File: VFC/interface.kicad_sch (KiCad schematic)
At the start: 5 parts, among them J2 Conn_01x06_Socket, J3 Conn_01x06_Socket, J4 Conn_01x03_Socket, J5 Conn_01x04_Socket, J6 SM08B-SRSS-TB_LF__SN_

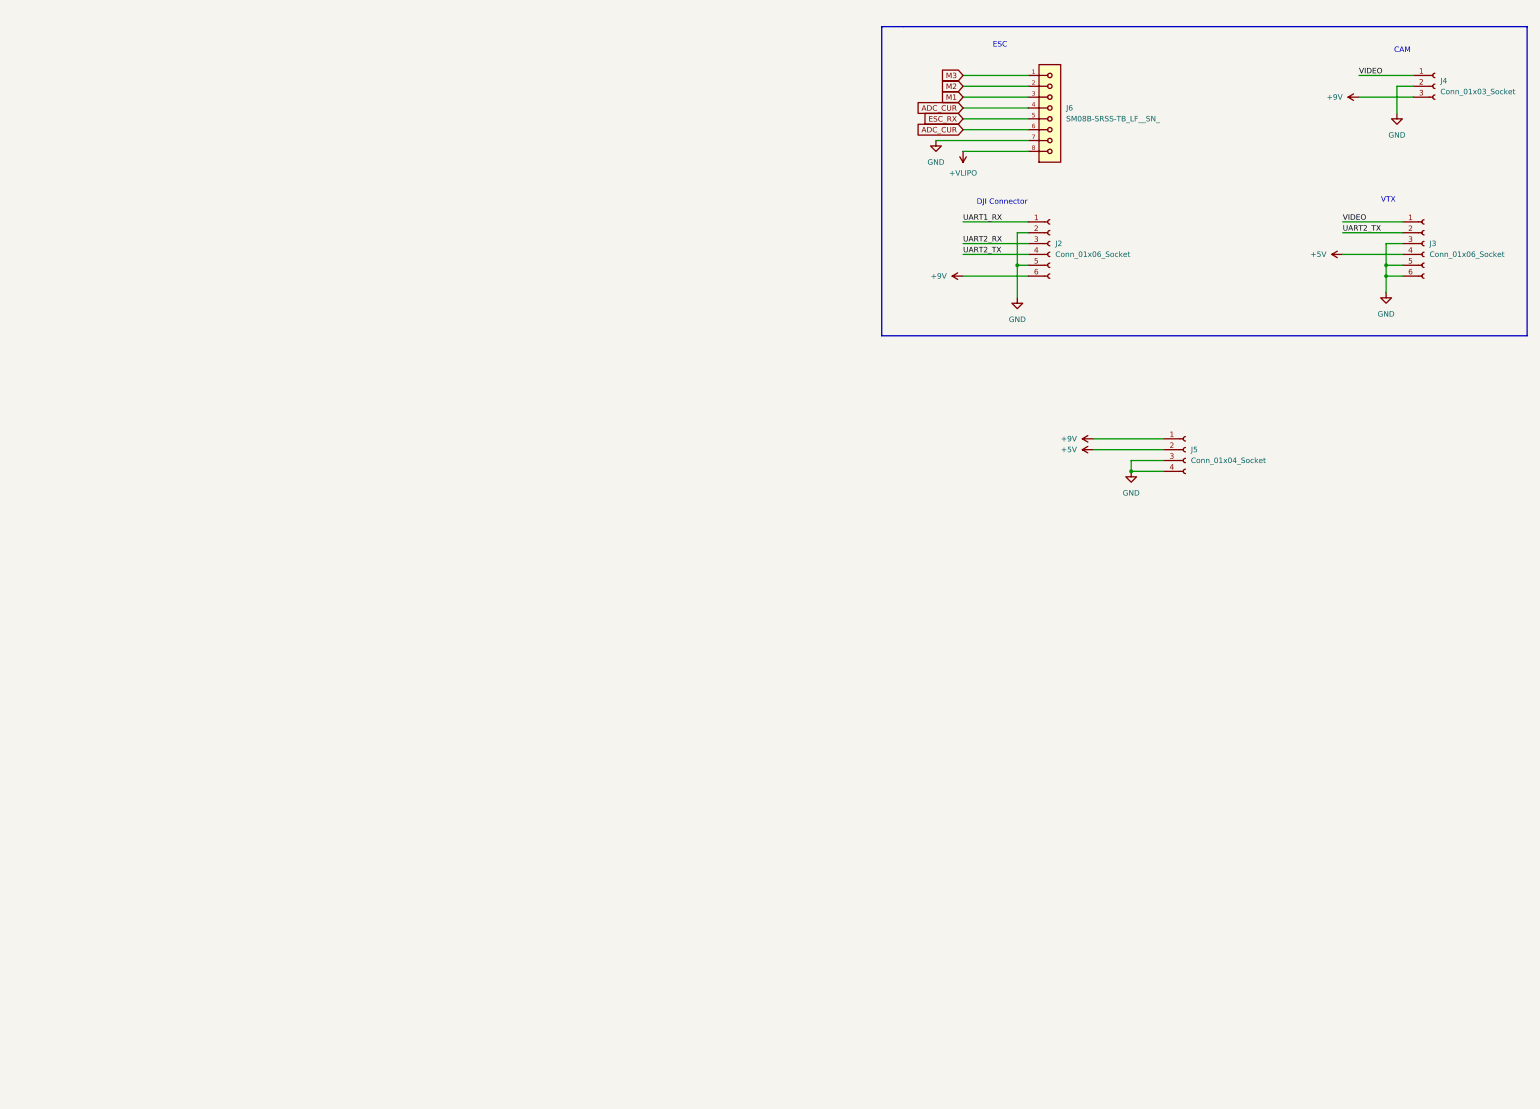
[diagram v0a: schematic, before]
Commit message: VFC PCB components placements complete
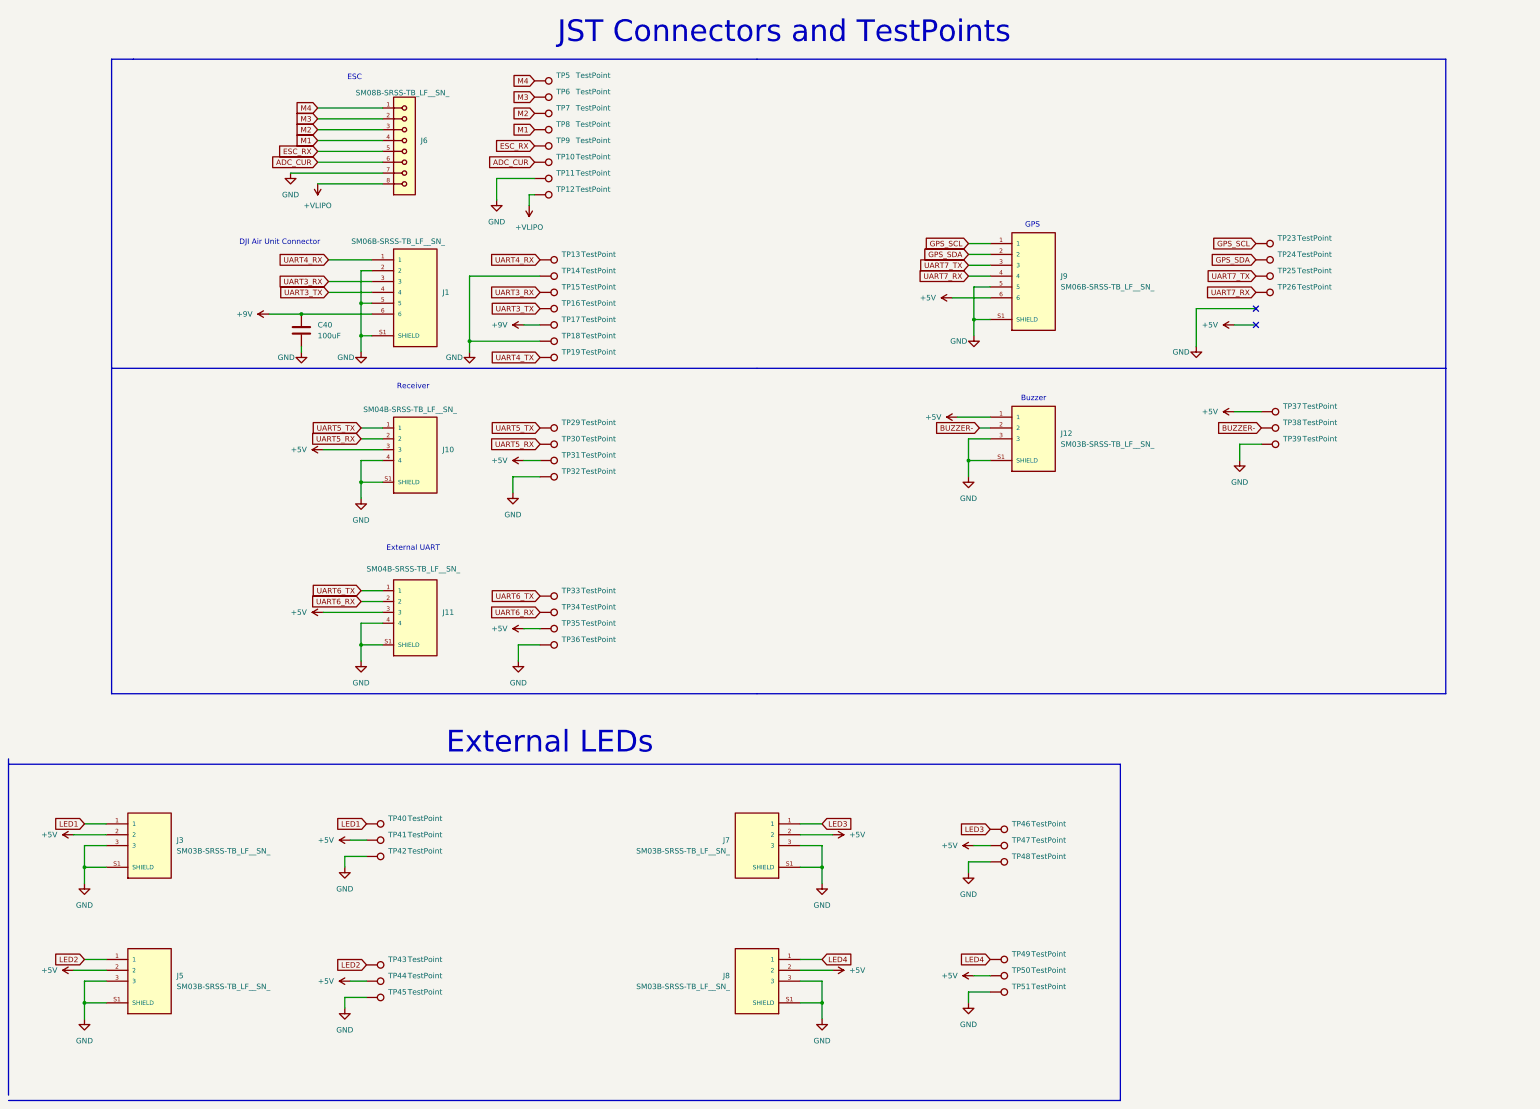
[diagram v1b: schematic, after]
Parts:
- removed J2, J3: Conn_01x06_Socket, Connector_JST:JST_SH_SM06B-SRSS-TB_1x06-1MP_P1.00mm_Horizontal, symbol Connector:Conn_01x06_Socket
- removed J4: Conn_01x03_Socket, Connector_JST:JST_SH_SM03B-SRSS-TB_1x03-1MP_P1.00mm_Horizontal, symbol Connector:Conn_01x03_Socket
- removed J5: Conn_01x04_Socket, symbol Connector:Conn_01x04_Socket
- added C40: 100uF, Capacitor_SMD:C_0603_1608Metric, symbol Device:C
- added J1, J9: SM06B-SRSS-TB_LF__SN_, SM06B-SRSS-TB_LF__SN_:JST_SM06B-SRSS-TB_LF__SN_, symbol SM06B-SRSS-TB_LF__SN_:SM06B-SRSS-TB_LF__SN_
- added J10, J11: SM04B-SRSS-TB_LF__SN_, SM04B-SRSS-TB_LF__SN_:JST_SM04B-SRSS-TB_LF__SN_, symbol SM04B-SRSS-TB_LF__SN_:SM04B-SRSS-TB_LF__SN_
- added J12, J3, J5, J7, J8: SM03B-SRSS-TB_LF__SN_, SM03B-SRSS-TB_LF__SN_:JST_SM03B-SRSS-TB_LF__SN_, symbol SM03B-SRSS-TB_LF__SN_:SM03B-SRSS-TB_LF__SN_
- added TP10, TP40, TP41, TP42, TP43, TP44, TP45, TP46, TP47, TP48, TP49, TP5, TP50, TP51, TP6, TP7, TP8, TP9: TestPoint, TestPoint:TestPoint_Pad_D1.0mm, symbol Connector:TestPoint
- added TP11, TP12: TestPoint, TestPoint:TestPoint_Pad_D2.0mm, symbol Connector:TestPoint
- added TP13, TP14, TP15, TP16, TP18, TP19, TP23, TP24, TP25, TP26, TP29, TP30, TP32, TP33, TP34, TP36, TP38, TP39: TestPoint, TestPoint:TestPoint_Pad_1.0x1.0mm, symbol Connector:TestPoint
- added TP17, TP31, TP35, TP37: TestPoint, TestPoint:TestPoint_Pad_2.0x2.0mm, symbol Connector:TestPoint
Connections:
- net +5V: now also J10.3, J11.3, J12.1, J3.2, J5.2, J7.2, J8.2, J9.6, TP31.1, TP35.1, TP37.1, TP41.1, TP44.1, TP47.1, TP50.1
- net +9V: now also C40.1, J1.6, TP17.1
- net +VLIPO: now also TP12.1
- net ADC_CUR: now also TP10.1; no longer J6.4
- net ESC_RX: now also TP9.1
- net GND: now also C40.2, J1.2, J1.5, J1.S1 (SHIELD), J1.S2 (SHIELD), J10.4, J10.S1 (SHIELD), J10.S2 (SHIELD), J11.4, J11.S1 (SHIELD), J11.S2 (SHIELD), J12.3, J12.S1 (SHIELD), J12.S2 (SHIELD), J3.3, J3.S1 (SHIELD), J3.S2 (SHIELD), J5.3, J5.S1 (SHIELD), J5.S2 (SHIELD), J7.3, J7.S1 (SHIELD), J7.S2 (SHIELD), J8.3, J8.S1 (SHIELD), J8.S2 (SHIELD), J9.5, J9.S1 (SHIELD), J9.S2 (SHIELD), TP11.1, TP14.1, TP18.1, TP32.1, TP36.1, TP39.1, TP42.1, TP45.1, TP48.1, TP51.1
- net M1: now also J6.4, TP8.1; no longer J6.3
- net M2: now also J6.3, TP7.1; no longer J6.2
- net M3: now also J6.2, TP6.1; no longer J6.1
- new net BUZZER-: J12.2, TP38.1
- new net GPS_SCL: J9.1, TP23.1
- new net GPS_SDA: J9.2, TP24.1
- new net LED1: J3.1, TP40.1
- new net LED2: J5.1, TP43.1
- new net LED3: J7.1, TP46.1
- new net LED4: J8.1, TP49.1
- new net M4: J6.1, TP5.1
- new net UART3_RX: J1.3, TP15.1
- new net UART3_TX: J1.4, TP16.1
- new net UART4_RX: J1.1, TP13.1
- new net UART4_TX: TP19.1
- new net UART5_RX: J10.2, TP30.1
- new net UART5_TX: J10.1, TP29.1
- new net UART6_RX: J11.2, TP34.1
- new net UART6_TX: J11.1, TP33.1
- new net UART7_RX: J9.4, TP26.1
- new net UART7_TX: J9.3, TP25.1
- no-connect marks 0 -> 2
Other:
- note added: "Buzzer"
- note added: "DJI Air Unit Connector"
- note added: "External LEDs"
- note added: "External UART"
- note added: "GPS"
- note added: "JST Connectors and TestPoints"
- note added: "Receiver"
- note removed: "CAM"
- note removed: "DJI Connector"
- note removed: "VTX"
- moved on the sheet: J6
